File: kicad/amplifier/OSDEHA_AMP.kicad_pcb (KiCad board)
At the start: 2 copper layers, 89 parts, among them J1 INPUT, J2 HEATERS DC, J3 PSU HV, J4 OUTPUT, J5 DHT FIL2, J6 DHT FIL1, Q1 DN2540N5-G, Q10 DN2540, Q2 DN2540N5-G, Q3 STF3LN80K5, Q4 STF3LN80K5, Q5 AOT1N60, Q6 IXTP3N100D2, Q7 AOT1N60, Q8 IXTP3N100D2, Q9 DN2540, SW1 SW_DPDT_x2, U1 6E5P, U2 6E5P, U3 801A, U4 801A

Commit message: up
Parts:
- R4, R9: footprint Resistor_THT:R_Axial_DIN0922_L20.0mm_D9.0mm_P7.62mm_Vertical -> Resistor_THT:R_Axial_Power_L25.0mm_W9.0mm_P27.94mm
- moved C2 75.0 mm to (-83.8, 61.4), turned to -90 degrees
- moved U1 46.0 mm to (-55.9, 105.6)
- moved R2 40.1 mm to (-42.3, 121.9), turned to 90 degrees
- moved R1 40.0 mm to (-42.3, 124.5), turned to -90 degrees
- moved R9 38.9 mm to (-101.6, 88.9)
- moved C3 28.8 mm to (-45.7, 59.9), turned to -90 degrees
- moved R3 20.3 mm to (-78.7, 124.5), turned to -90 degrees
- moved R4 9.46 mm to (-63.5, 87.6)
- moved J1 9.03 mm to (-57.0, 132.1)
- moved R7 8.82 mm to (-78.7, 111.8), turned to -90 degrees
- moved U2 2.41 mm to (-93.9, 106.9)
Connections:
- C6 pad 2: /Buffer_CCS_load1/NEG -> Net-(J3-Pin_3)
- C7 pad 2: Net-(J3-Pin_3) -> /Buffer_CCS_load1/NEG

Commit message: amp pcb
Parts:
- R10: footprint Resistor_THT:R_Axial_Power_L25.0mm_W9.0mm_P7.62mm_Vertical -> Resistor_THT:R_Axial_Power_L25.0mm_W9.0mm_P30.48mm
- R25, R26, R29: footprint Resistor_THT:R_Axial_DIN0207_L6.3mm_D2.5mm_P10.16mm_Horizontal -> Resistor_THT:R_Axial_DIN0207_L6.3mm_D2.5mm_P2.54mm_Vertical
- moved D14 256.1 mm to (31.8, 25.4), turned to -90 degrees
- moved D12 249.5 mm to (68.6, 24.8), turned to -90 degrees
- moved D13 249.0 mm to (39.4, 25.4), turned to -90 degrees
- moved D11 248.5 mm to (61.0, 24.8), turned to -90 degrees
- moved R40 221.6 mm to (64.8, 34.3), turned to 90 degrees
- moved R39 215.3 mm to (116.8, 24.1)
- moved R37 215.2 mm to (131.4, 24.8)
- moved R38 213.3 mm to (138.4, 29.8), turned to -90 degrees
- moved R36 206.7 mm to (131.4, 21.0)
- moved R35 206.5 mm to (131.4, 17.1)
- moved R34 203.9 mm to (83.2, 24.1)
- moved D7 195.2 mm to (92.7, 31.8), turned to 180 degrees
- moved D8 194.4 mm to (92.7, 36.8), turned to 180 degrees
- moved D9 193.2 mm to (127.0, 31.8), turned to 180 degrees
- moved D10 192.3 mm to (127.0, 36.8), turned to 180 degrees
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
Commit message: up
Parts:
- R4, R9: footprint Resistor_THT:R_Axial_Power_L25.0mm_W9.0mm_P27.94mm -> Resistor_THT:R_Radial_Power_L16.1mm_W9.0mm_P7.37mm
- moved R9 20.8 mm to (-25.4, 58.2)
- moved C2 13.5 mm to (-40.6, 34.5)
- moved C8 7.74 mm to (91.7, 47.0)
- moved R4 6.90 mm to (-12.7, 58.4)
- moved R14 6.84 mm to (25.4, 53.3), turned to 0 degrees
- moved C3 6.02 mm to (2.54, 34.5)
- moved R26 4.92 mm to (113.0, 80.6)
- moved R29 4.92 mm to (85.2, 80.6)
- moved C5 4.92 mm to (134.3, 67.9)
- moved C6 4.92 mm to (106.7, 67.9)
- moved R25 4.92 mm to (140.9, 80.6)
- moved C7 4.76 mm to (78.4, 68.6)
- moved C1 4.49 mm to (31.9, 47.0)
- moved D12 3.93 mm to (72.5, 24.8)
- moved R20 3.93 mm to (81.4, 39.4)
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
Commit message: up
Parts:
- added H5: VENTILATION, MountingHole:MountingHole_5mm, F.Cu at (-30.5, 39.4)
- R10: footprint Resistor_THT:R_Axial_Power_L25.0mm_W9.0mm_P30.48mm -> Resistor_THT:R_Radial_Power_L16.1mm_W9.0mm_P7.37mm
- moved R10 59.9 mm to (-22.7, 39.4)
- moved R15 21.9 mm to (47.0, 39.4)
- moved R1 7.62 mm to (22.2, 82.5)
- moved R2 7.62 mm to (17.1, 82.5)
- moved U2 3.19 mm to (-39.3, 80.2)
- moved C8 2.54 mm to (94.2, 47.0)
- moved C7 1.91 mm to (78.4, 66.7)
- moved J1 1.91 mm to (-17.1, 88.2)
- moved J2 1.91 mm to (36.8, 88.3)
- moved J3 1.91 mm to (138.7, 88.9)
- moved J4 1.91 mm to (114.9, 88.9)
- moved J5 1.91 mm to (80.8, 88.2)
- moved J6 1.91 mm to (50.8, 88.4)
- moved R25 1.91 mm to (140.9, 78.7)
- moved R26 1.91 mm to (113.0, 78.7)
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
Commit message: amp pcb
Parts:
- R15, R20: footprint Resistor_THT:R_Axial_DIN0207_L6.3mm_D2.5mm_P10.16mm_Horizontal -> Resistor_THT:R_Axial_DIN0207_L6.3mm_D2.5mm_P2.54mm_Vertical
- moved C2 208.1 mm to (158.5, 95.0), turned to 180 degrees
- moved C3 173.3 mm to (158.5, 110.0), turned to 180 degrees
- moved R10 140.6 mm to (116.1, 61.5), turned to 90 degrees
- moved R4 127.6 mm to (113.5, 76.8), turned to 180 degrees
- moved U2 125.1 mm to (84.1, 100.3), turned to -90 degrees
- moved J1 123.1 mm to (100.4, 125.0)
- moved Q2 120.9 mm to (76.1, 53.3)
- moved R8 120.9 mm to (73.5, 59.7)
- moved R19 120.0 mm to (177.7, 73.0), turned to 180 degrees
- moved R14 119.6 mm to (143.4, 73.0), turned to 180 degrees
- moved D1 119.0 mm to (100.8, 53.3)
- moved D2 119.0 mm to (100.8, 57.8)
- moved Q1 119.0 mm to (94.2, 53.3)
- moved R5 119.0 mm to (89.4, 63.5)
- moved R6 119.0 mm to (104.0, 63.5)
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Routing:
- added copper zone on F.Cu, net GND
- removed copper zone on B.Cu, net GND

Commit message: amp pcb
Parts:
- moved J2 12.1 mm to (135.0, 125.0)
- moved D14 7.90 mm to (150.0, 58.5)
- moved R4 7.27 mm to (106.3, 76.0), turned to 0 degrees
- moved D13 7.26 mm to (142.5, 58.5)
- moved R7 4.29 mm to (76.7, 116.0)
- moved U2 4.15 mm to (80.0, 100.0)
- moved R29 3.95 mm to (194.0, 116.0)
- moved R26 3.84 mm to (222.0, 116.0)
- moved R25 3.82 mm to (250.0, 116.0)
- moved R3 3.66 mm to (84.0, 126.2)
- moved J1 2.89 mm to (97.5, 125.0)
- moved R10 2.87 mm to (118.1, 63.5)
- moved R14 2.62 mm to (146.0, 73.0)
- moved U1 2.32 mm to (110.0, 100.0)
- moved R15 2.32 mm to (156.5, 73.0)
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
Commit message: up
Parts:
- removed D1, D11, D12, D13, D14, D2: 15V, Diode_THT:D_DO-41_SOD81_P7.62mm_Horizontal
- R34, R39: value 1k -> 300
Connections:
- Q1 pad 1: Net-(D1-K) -> Net-(Q1-G)
- Q10 pad 2: Net-(D13-K) -> Net-(Q10-G)
- Q9 pad 2: Net-(D11-K) -> Net-(Q9-G)
- R40 pad 1: /Buffer_CCS_load1/NEG -> Net-(Q9-G)
- R40 pad 2: Net-(D11-K) -> /Buffer_CCS_load1/NEG
- R42 pad 1: /Buffer_CCS_load1/NEG -> Net-(Q10-G)
- R42 pad 2: Net-(D13-K) -> /Buffer_CCS_load1/NEG
- R5 pad 1: Net-(R10-Pad1) -> Net-(Q1-G)
- R5 pad 2: Net-(D1-K) -> Net-(R10-Pad1)

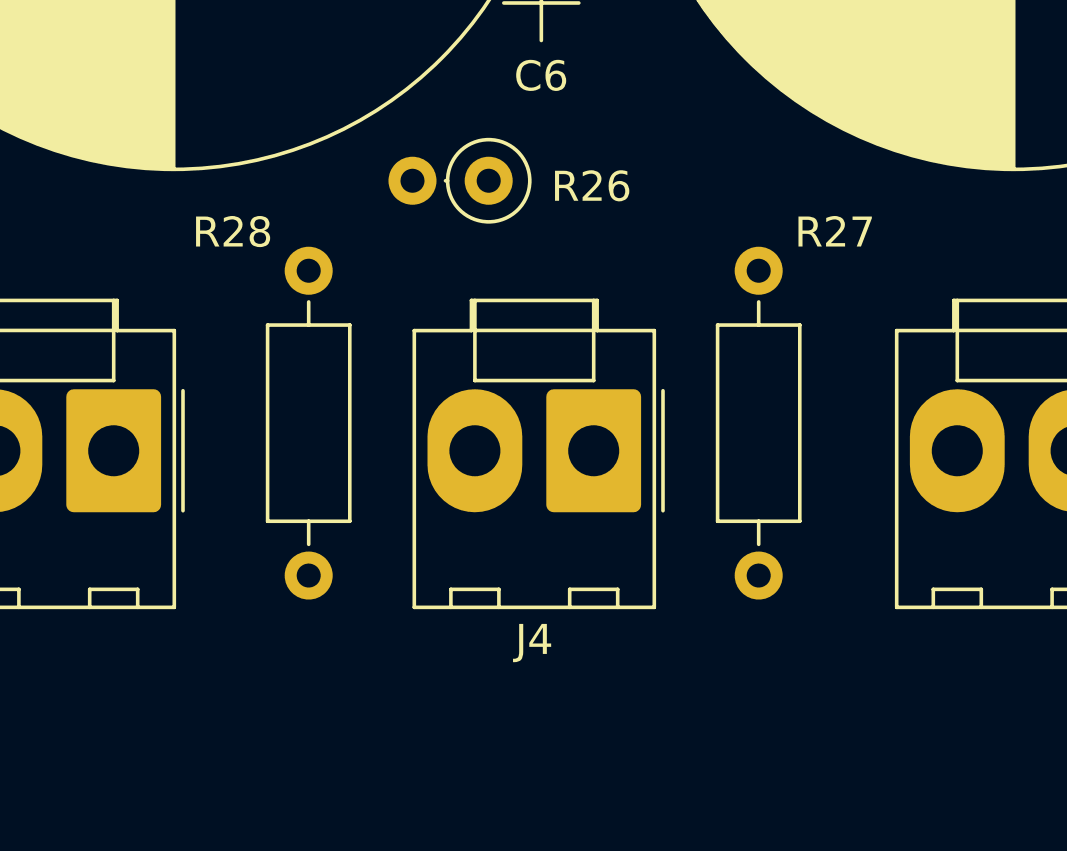
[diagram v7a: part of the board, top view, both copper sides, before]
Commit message: safety resistors
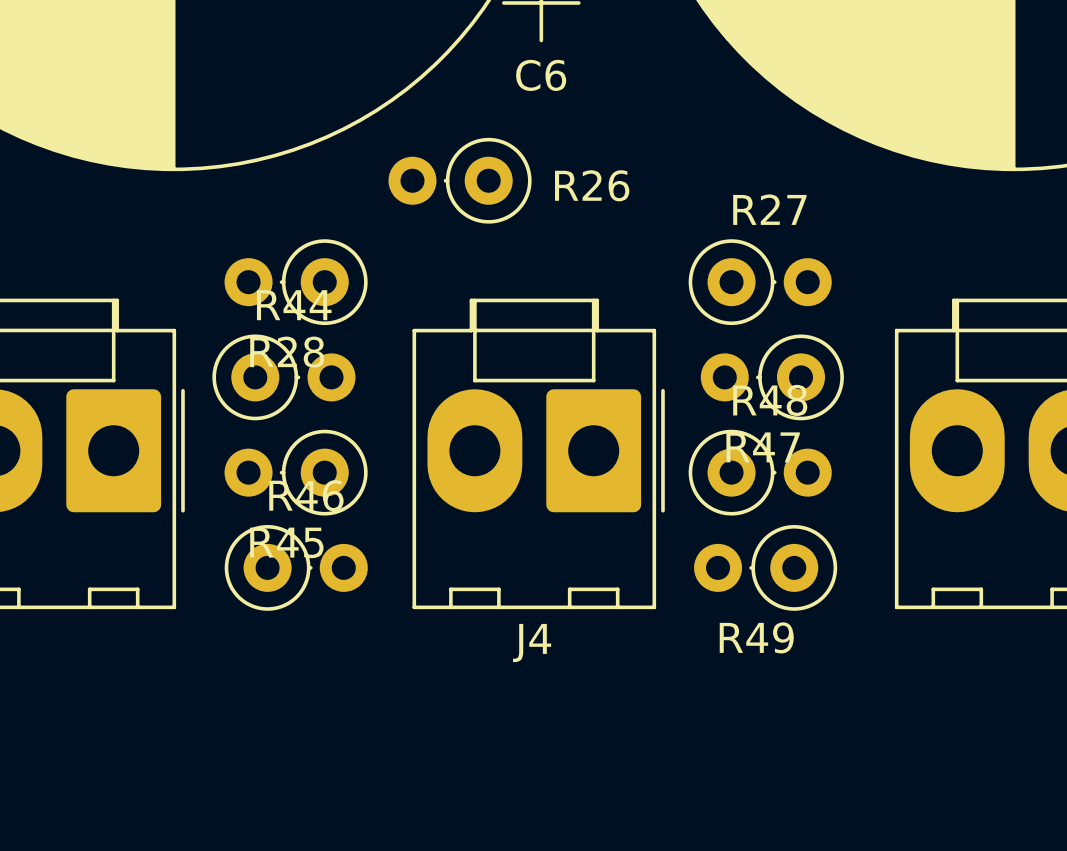
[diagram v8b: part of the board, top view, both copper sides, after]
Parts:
- added R44: 1.27k, Resistor_THT:R_Axial_DIN0207_L6.3mm_D2.5mm_P2.54mm_Vertical, F.Cu at (214.2, 122.6)
- added R45: 1.27k, Resistor_THT:R_Axial_DIN0207_L6.3mm_D2.5mm_P2.54mm_Vertical, F.Cu at (216.5, 125.7)
- added R46: 1.27k, Resistor_THT:R_Axial_DIN0207_L6.3mm_D2.5mm_P2.54mm_Vertical, F.Cu at (214.6, 128.9)
- added R47: 1.27k, Resistor_THT:R_Axial_DIN0207_L6.3mm_D2.5mm_P2.54mm_Vertical, F.Cu at (232.4, 122.6)
- added R48: 1.27k, Resistor_THT:R_Axial_DIN0207_L6.3mm_D2.5mm_P2.54mm_Vertical, F.Cu at (230.1, 125.7)
- added R49: 1.27k, Resistor_THT:R_Axial_DIN0207_L6.3mm_D2.5mm_P2.54mm_Vertical, F.Cu at (232.2, 128.9)
- R27, R28: value 5.1k -> 1.27k; footprint Resistor_THT:R_Axial_DIN0207_L6.3mm_D2.5mm_P10.16mm_Horizontal -> Resistor_THT:R_Axial_DIN0207_L6.3mm_D2.5mm_P2.54mm_Vertical
- moved R27 0.98 mm to (230.1, 119.4), turned to 0 degrees
- moved R28 0.66 mm to (216.5, 119.4), turned to 180 degrees
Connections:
- R27 pad 2: Net-(J4-Pin_1) -> Net-(R27-Pad2)
- R28 pad 2: Net-(J4-Pin_2) -> Net-(R28-Pad2)
